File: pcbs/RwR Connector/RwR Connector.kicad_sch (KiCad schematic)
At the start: 4 parts, among them J101 Conn_02x20_Odd_Even, J102 Conn_02x20_Odd_Even, J103 Conn_01x04, J104 Conn_02x20_Odd_Even

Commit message: Routing
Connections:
- no-connect marks 4 -> 48
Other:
- title: (none) -> Register with Reset Test Connector
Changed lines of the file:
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@@
 	(generator_version "8.0")
 	(paper "A4")
+	(title_block
+		(title "Register with Reset Test Connector")
+		(rev "0")
+	)
 	(junction
 		(at 54.61 106.68)
@@
 	)
 	(no_connect
+		(at 52.07 125.73)
+	)
+	(no_connect
+		(at 64.77 128.27)
+	)
+	(no_connect
+		(at 53.34 67.31)
+	)
+	(no_connect
+		(at 53.34 87.63)
+	)
+	(no_connect
+		(at 52.07 128.27)
+	)
+	(no_connect
+		(at 64.77 171.45)
+	)
+	(no_connect
+		(at 53.34 72.39)
+	)
+	(no_connect
+		(at 52.07 135.89)
+	)
+	(no_connect
+		(at 53.34 82.55)
+	)
+	(no_connect
+		(at 66.04 77.47)
+	)
+	(no_connect
+		(at 53.34 69.85)
+	)
+	(no_connect
 		(at 144.78 97.79)
+	)
+	(no_connect
+		(at 52.07 123.19)
+	)
+	(no_connect
+		(at 52.07 133.35)
+	)
+	(no_connect
+		(at 53.34 77.47)
+	)
+	(no_connect
+		(at 64.77 130.81)
+	)
+	(no_connect
+		(at 64.77 125.73)
+	)
+	(no_connect
+		(at 64.77 135.89)
+	)
+	(no_connect
+		(at 64.77 140.97)
+	)
+	(no_connect
+		(at 66.04 74.93)
+	)
+	(no_connect
+		(at 64.77 148.59)
+	)
+	(no_connect
+		(at 66.04 85.09)
+	)
+	(no_connect
+		(at 52.07 148.59)
+	)
+	(no_connect
+		(at 66.04 69.85)
+	)
+	(no_connect
+		(at 52.07 130.81)
+	)
+	(no_connect
+		(at 64.77 133.35)
 	)
 	(no_connect
@@
 	)
 	(no_connect
+		(at 52.07 143.51)
+	)
+	(no_connect
+		(at 53.34 80.01)
+	)
+	(no_connect
+		(at 66.04 80.01)
+	)
+	(no_connect
+		(at 64.77 143.51)
+	)
+	(no_connect
+		(at 53.34 74.93)
+	)
+	(no_connect
+		(at 64.77 146.05)
+	)
+	(no_connect
+		(at 66.04 39.37)
+	)
+	(no_connect
+		(at 53.34 85.09)
+	)
+	(no_connect
+		(at 66.04 72.39)
+	)
+	(no_connect
+		(at 53.34 64.77)
+	)
+	(no_connect
 		(at 144.78 100.33)
 	)
 	(no_connect
+		(at 52.07 140.97)
+	)
+	(no_connect
+		(at 64.77 138.43)
+	)
+	(no_connect
+		(at 52.07 171.45)
+	)
+	(no_connect
+		(at 66.04 67.31)
+	)
+	(no_connect
+		(at 52.07 146.05)
+	)
+	(no_connect
+		(at 66.04 82.55)
+	)
+	(no_connect
+		(at 64.77 123.19)
+	)
+	(no_connect
+		(at 53.34 62.23)
+	)
+	(no_connect
+		(at 52.07 138.43)
+	)
+	(no_connect

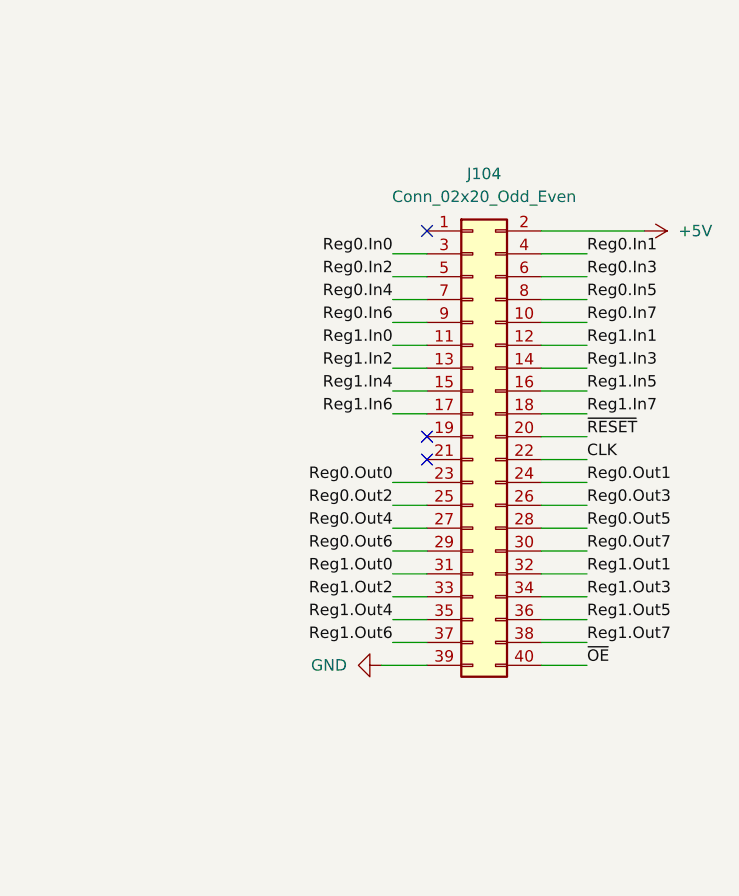
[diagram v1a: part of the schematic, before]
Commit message: Revise the Register with Reset (#3)
Updates to Register-with-Reset:

- Convert to edge connector
- Route clock through an 'AND' with the Reset line, so the clock doesn't block reset
- Shrink the board somewhat by repositioning components
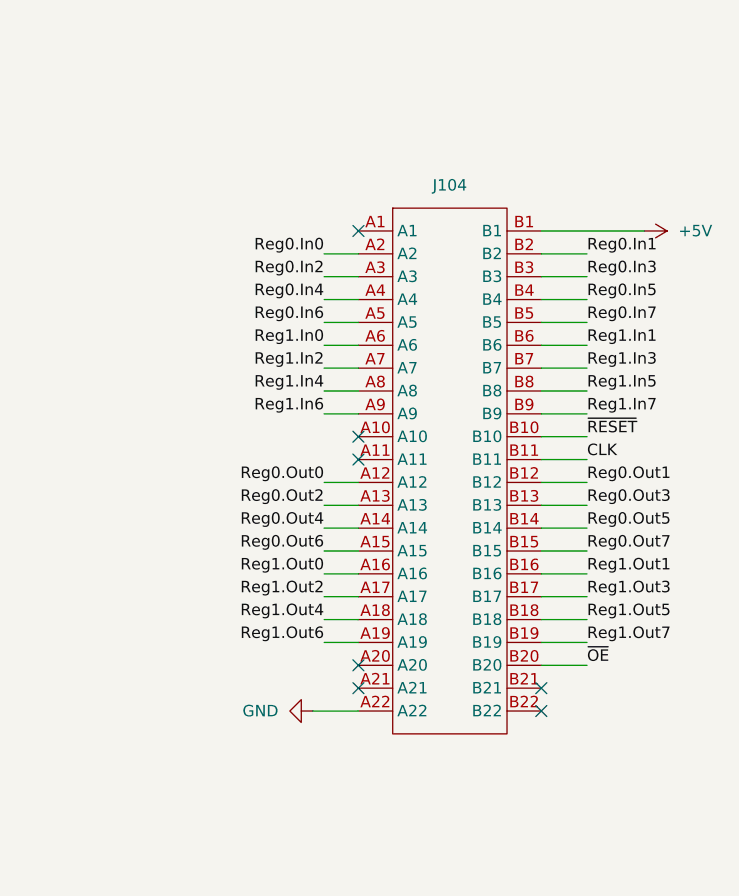
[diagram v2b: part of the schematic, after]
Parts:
- removed J104: Conn_02x20_Odd_Even, Connector_PinHeader_2.54mm:PinHeader_2x20_P2.54mm_Vertical, symbol Connector_Generic:Conn_02x20_Odd_Even
- added J104: ~, BoardEdgeConnectors:TE-5530843-4-Mount, symbol BoardEdgeConnectors:TE-5530843-4
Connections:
- net +5V: now also J104.B1
- net CLK: now also J104.B11
- net GND: now also J104.A22
- net Reg0.In0: now also J104.A2
- net Reg0.In1: now also J104.B2
- net Reg0.In2: now also J104.A3
- net Reg0.In3: now also J104.B3
- net Reg0.In4: now also J104.A4
- net Reg0.In5: now also J104.B4
- net Reg0.In6: now also J104.A5
- net Reg0.In7: now also J104.B5
- net Reg0.Out0: now also J104.A12
- net Reg0.Out1: now also J104.B12
- net Reg0.Out2: now also J104.A13
- net Reg0.Out3: now also J104.B13
- net Reg0.Out4: now also J104.A14
- net Reg0.Out5: now also J104.B14
- net Reg0.Out6: now also J104.A15
- net Reg0.Out7: now also J104.B15
- net Reg1.In0: now also J104.A6
- net Reg1.In1: now also J104.B6
- net Reg1.In2: now also J104.A7
- net Reg1.In3: now also J104.B7
- net Reg1.In4: now also J104.A8
- net Reg1.In5: now also J104.B8
- net Reg1.In6: now also J104.A9
- net Reg1.In7: now also J104.B9
- net Reg1.Out0: now also J104.A16
- net Reg1.Out1: now also J104.B16
- net Reg1.Out2: now also J104.A17
- net Reg1.Out3: now also J104.B17
- net Reg1.Out4: now also J104.A18
- net Reg1.Out5: now also J104.B18
- net Reg1.Out6: now also J104.A19
- net Reg1.Out7: now also J104.B19
- net ~{OE}: now also J104.B20
- net ~{RESET}: now also J104.B10
- no-connect marks 48 -> 52
